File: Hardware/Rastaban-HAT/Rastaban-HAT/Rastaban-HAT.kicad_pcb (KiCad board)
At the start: 2 copper layers, 84.3 x 85.4 mm, 94 parts, among them IC1 BCR420UW6-7, IC2 BCM53DS, J1 1778780, J10 GPIO, J11 Conn_01x06_Male, J2 1778780, J3 1778780, J4 Screw_Terminal_01x02, J5 Jack-DC 12V+, J6 SM04B-SRSS-TB(LF)(SN)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

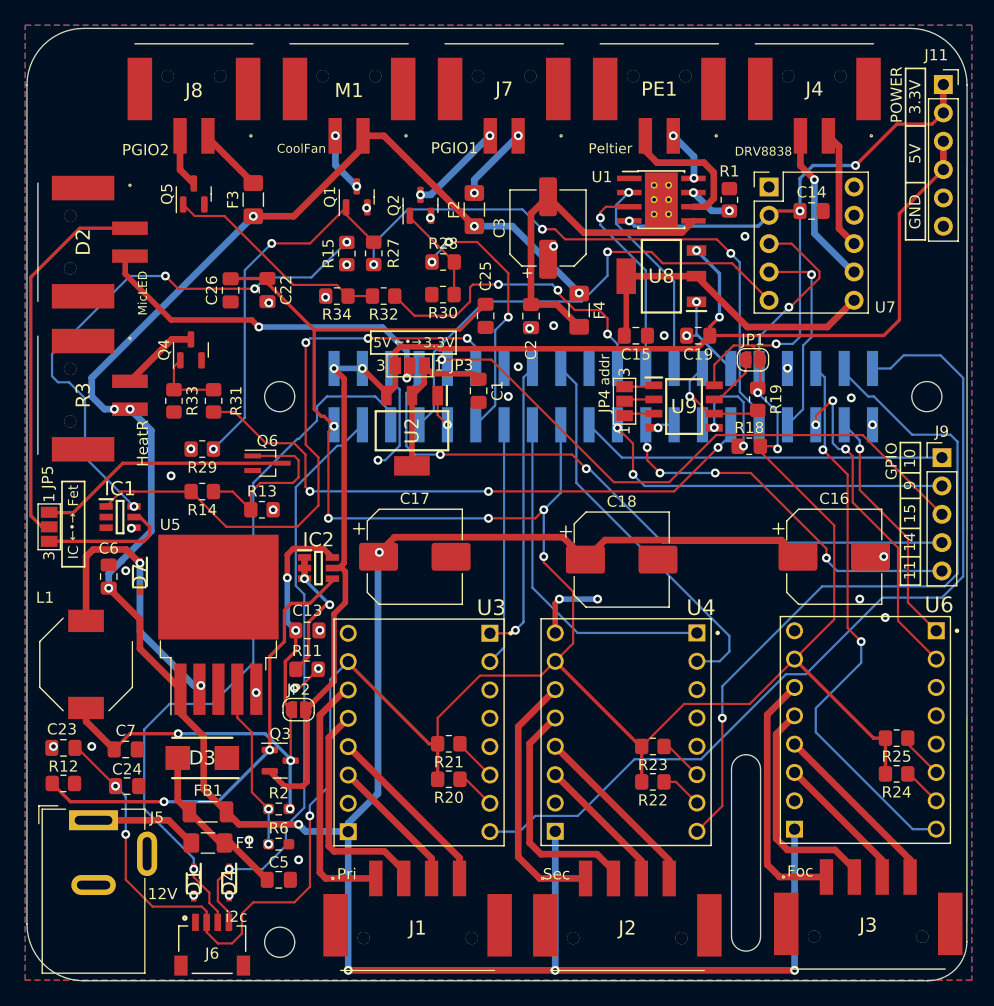
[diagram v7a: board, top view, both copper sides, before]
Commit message: improved traces
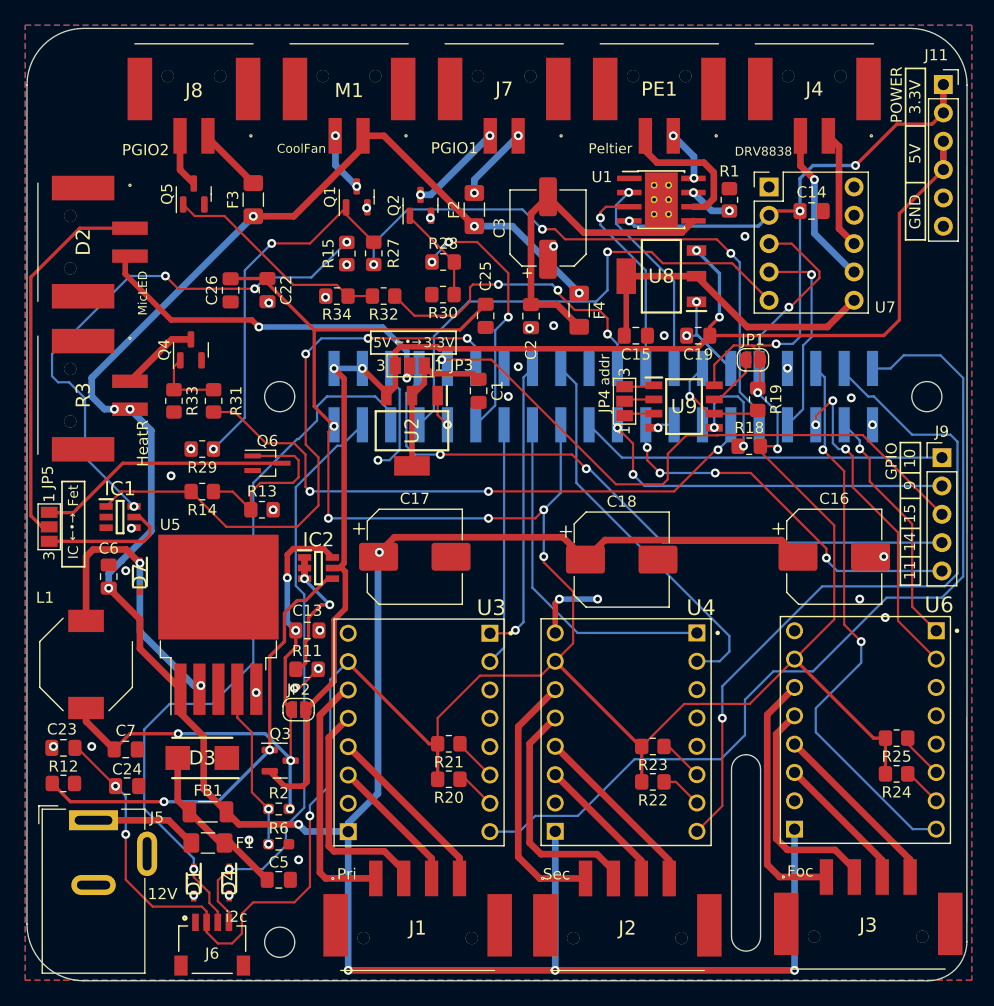
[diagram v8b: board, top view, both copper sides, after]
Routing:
- net ENPRI: track 79.1 -> 81.0 mm
- net SLEEP: track 43.9 -> 45.5 mm
- net GPIO15: track 54.1 -> 55.6 mm
- net CTRLLED: track 54.4 -> 53.8 mm
